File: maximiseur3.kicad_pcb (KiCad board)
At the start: 2 copper layers, 150 x 100 mm, 45 parts, among them J1 PV+/M+, J2 M-, J3 PV-, P1 SW SW, Q1 IRLB3036G, Q2 IRLB3036G, Q3 IRLB3036G, Q4 IRLB3036G, T1 BD139, U1 LM311

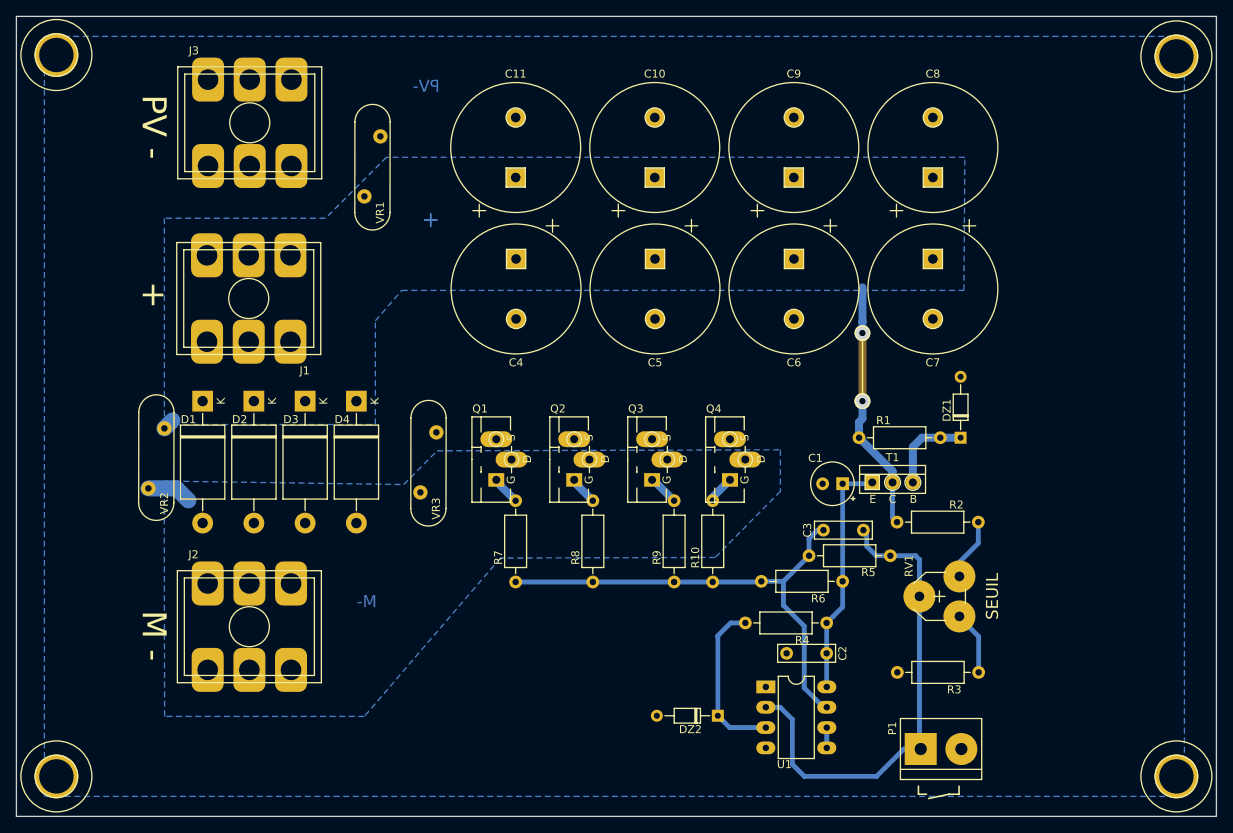
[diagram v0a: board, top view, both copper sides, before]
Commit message: ajout seconde empreinte pour le potentiomètre + pads plus larges + sérigraphie
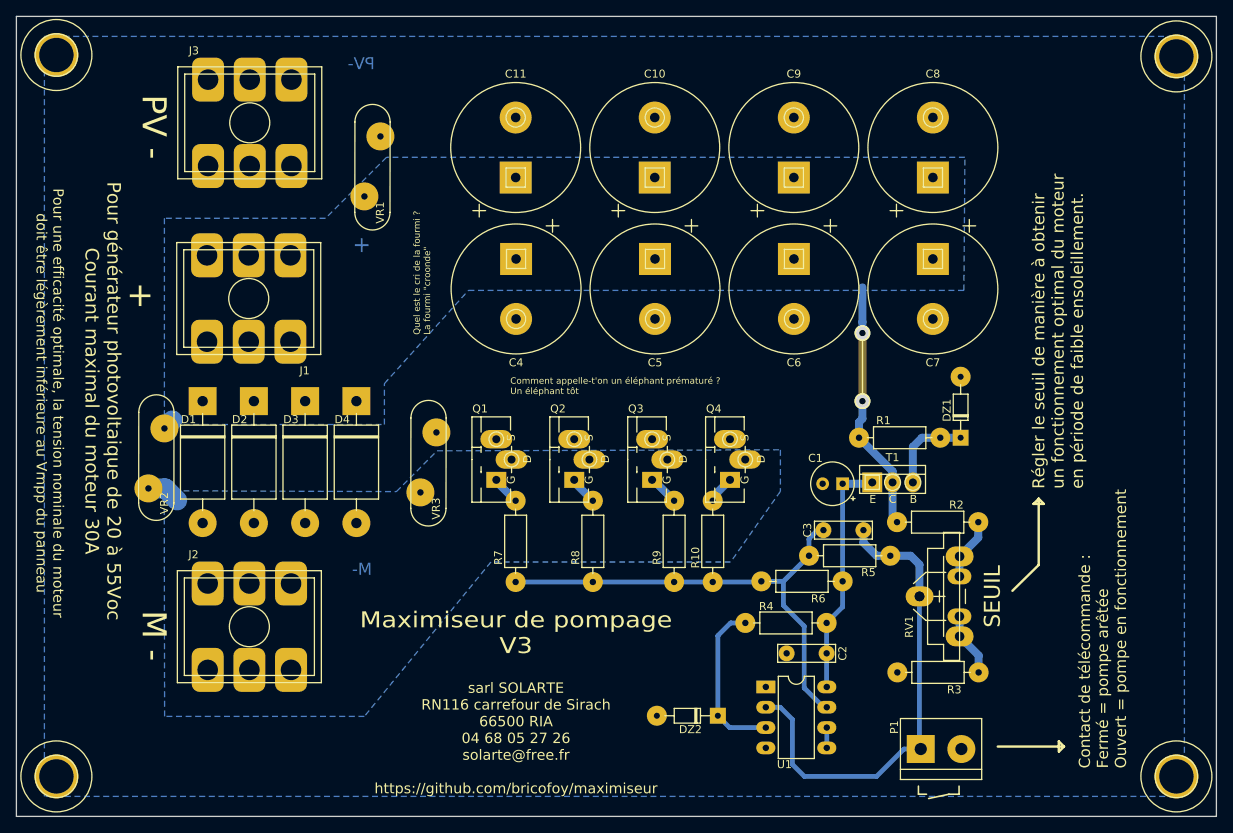
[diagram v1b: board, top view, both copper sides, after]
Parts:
- added Rv1: 2k, maximiseur:pot_vert_Radiohm, F.Cu at (149.5, 107.0)
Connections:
- RV1 pad 1: Net-(R2-Pad2) -> Net-(R3-Pad1)
- RV1 pad 3: Net-(R3-Pad1) -> Net-(R2-Pad2)
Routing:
- net Net-(R2-Pad2): track 7.76 -> 9.54 mm
- net /RC: track 58.9 -> 60.5 mm
- net /M-: track 5.62 -> 4.22 mm
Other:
- board text added: "Comment appelle-t'on un éléphant prématuré ? Un éléphant tôt"
- board text added: "Contact de télécommande : Fermé = pompe arêtée Ouvert = pompe en fonctionnement"
- board text added: "Maximiseur de pompage V3"
- board text added: "Pour générateur photovoltaique de 20 à 55Voc Courant maximal du moteur 30A"
- board text added: "Pour une efficacité optimale, la tension nominale du moteur doit être légèrement inférieure au Vmpp du panneau"
- board text added: "Quel est le cri de la fourmi ? La fourmi "croonde""
- board text added: "Régler le seuil de manière à obtenir un fonctionnement optimal du moteur en période de faible ensoleillement."
- board text added: "sarl SOLARTE RN116 carrefour de Sirach 66500 RIA 04 68 05 27 26 solarte@free.fr https://github.com/bricofoy/maximiseur"
